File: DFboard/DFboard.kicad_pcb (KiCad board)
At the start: 2 copper layers, 63.5 x 157.5 mm, 20 parts, among them J1 HFBR-2522ETZ, J10 HFBR-1522ETZ, J11 HFBR-2522ETZ, J12 HFBR-1522ETZ, J13 110-43-648-41-001000, J2 HFBR-1522ETZ, J3 HFBR-2522ETZ, J4 HFBR-1522ETZ, J5 HFBR-2522ETZ, J6 HFBR-1522ETZ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

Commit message: Added test points to schematic.  Started pcb layout.
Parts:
- removed J10, J12, J4, J6, J8: HFBR-1522ETZ, OptoDevice:Broadcom_AFBR-16xxZ_Horizontal
- removed J11, J3, J5, J7, J9: HFBR-2522ETZ, OptoDevice:Broadcom_AFBR-16xxZ_Horizontal
- removed R1, R2, R3, R4, R5, R6: 50, Resistor_THT:R_Axial_DIN0207_L6.3mm_D2.5mm_P7.62mm_Horizontal
- added JP1: Jumper3, Connector_PinHeader_2.54mm:PinHeader_1x03_P2.54mm_Vertical, F.Cu at (45.5, 27.5)
- added JP2: Jumper_3_Bridged12, Connector_PinHeader_2.54mm:PinHeader_1x03_P2.54mm_Vertical, F.Cu at (59.0, 33.0)
- added JP3: Jumper3, Connector_PinHeader_2.54mm:PinHeader_1x03_P2.54mm_Vertical, F.Cu at (99.0, 44.0)
- added JP4: Jumper3, Connector_PinHeader_2.54mm:PinHeader_1x03_P2.54mm_Vertical, F.Cu at (128.0, 49.5)
- added JP5: Jumper_3_Bridged12, Connector_PinHeader_2.54mm:PinHeader_1x03_P2.54mm_Vertical, F.Cu at (111.0, 45.0)
- added JP6: Jumper_3_Bridged12, Connector_PinHeader_2.54mm:PinHeader_1x03_P2.54mm_Vertical, F.Cu at (139.5, 47.0)
- added JP7: Jumper_3_Bridged12, Connector_PinHeader_2.54mm:PinHeader_1x03_P2.54mm_Vertical, F.Cu at (168.0, 56.0)
- added JP8: Jumper_2_Bridged, Connector_PinHeader_2.54mm:PinHeader_1x02_P2.54mm_Vertical, F.Cu at (81.2, 43.0)
- added JP9: Jumper_2_Bridged, Connector_PinHeader_2.54mm:PinHeader_1x02_P2.54mm_Vertical, F.Cu at (81.2, 38.5)
- added TP1: RX1, Connector_PinHeader_2.54mm:PinHeader_1x01_P2.54mm_Vertical, F.Cu at (66.5, 98.0)
- added TP10: RX8, Connector_PinHeader_2.54mm:PinHeader_1x01_P2.54mm_Vertical, F.Cu at (166.5, 98.0)
- added TP11: RX6, Connector_PinHeader_2.54mm:PinHeader_1x01_P2.54mm_Vertical, F.Cu at (103.0, 98.0)
- added TP12: RX5, Connector_PinHeader_2.54mm:PinHeader_1x01_P2.54mm_Vertical, F.Cu at (71.0, 98.0)
- added TP13: TX6, Connector_PinHeader_2.54mm:PinHeader_1x01_P2.54mm_Vertical, F.Cu at (104.5, 169.5)
- added TP14: TX5, Connector_PinHeader_2.54mm:PinHeader_1x01_P2.54mm_Vertical, F.Cu at (138.5, 147.0)
- added TP2: TX1, Connector_PinHeader_2.54mm:PinHeader_1x01_P2.54mm_Vertical, F.Cu at (61.5, 98.0)
- added TP3: RX2, Connector_PinHeader_2.54mm:PinHeader_1x01_P2.54mm_Vertical, F.Cu at (98.5, 98.0)
- added TP4: TX2, Connector_PinHeader_2.54mm:PinHeader_1x01_P2.54mm_Vertical, F.Cu at (93.5, 98.0)
- added TP5: RX3, Connector_PinHeader_2.54mm:PinHeader_1x01_P2.54mm_Vertical, F.Cu at (132.0, 97.5)
- added TP6: TX3, Connector_PinHeader_2.54mm:PinHeader_1x01_P2.54mm_Vertical, F.Cu at (127.0, 97.5)
- added TP7: RX4, Connector_PinHeader_2.54mm:PinHeader_1x01_P2.54mm_Vertical, F.Cu at (162.0, 98.0)
- added TP8: TX4, Connector_PinHeader_2.54mm:PinHeader_1x01_P2.54mm_Vertical, F.Cu at (156.5, 98.0)
- added TP9: RX7, Connector_PinHeader_2.54mm:PinHeader_1x01_P2.54mm_Vertical, F.Cu at (136.5, 97.5)
- added U2: ~, Misc:Max3232, F.Cu at (46.6, 74.8)
- added U3: ~, Misc:Max3232, F.Cu at (78.0, 75.0)
- added U4: ~, Misc:Max3232, F.Cu at (111.5, 75.0)
- added U5: ~, Misc:Max3232, F.Cu at (141.4, 75.5)
- added U6: Power, Misc:PowerPal, F.Cu at (271.5, 123.0)
- J1: value HFBR-2522ETZ -> DB25_Plug_MountingHoles_Male; footprint OptoDevice:Broadcom_AFBR-16xxZ_Horizontal -> Connector_Dsub:DSUB-25_Male_Horizontal_P2.77x2.84mm_EdgePinOffset4.94mm_Housed_MountingHolesOffset7.48mm
- J2: value HFBR-1522ETZ -> DB25_Receptacle_MountingHoles_Female; footprint OptoDevice:Broadcom_AFBR-16xxZ_Horizontal -> Connector_Dsub:DSUB-25_Female_Horizontal_P2.77x2.84mm_EdgePinOffset4.94mm_Housed_MountingHolesOffset7.48mm
- moved J2 127.0 mm to (179.7, 27.9), turned to 90 degrees
- moved J13 108.2 mm to (136.0, 117.3), turned to -90 degrees
- moved U1 43.5 mm to (54.0, 96.0)
- moved J1 22.6 mm to (30.8, 28.4), turned to -90 degrees
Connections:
- J1 pad 1: /RX1 -> Net-(U2-R1_In)
- J1 pad 2: Net-(J1-Pad2) -> unconnected-(J1-Pad2)
- J1 pad 3: Net-(U1-Pad10) -> Net-(U3-R1_In)
- J1 pad 4: /RX1 -> unconnected-(J1-Pad4)
- J1 pad 5: (no net) -> Net-(JP9-B)
- J1 pad 8: (no net) -> Net-(JP5-C)
- J13 pad 1: Net-(J1-Pad2) -> Net-(J13-Pad1)
- J13 pad 16: /TX6 -> Net-(J13-Pad16)
- J13 pad 20: unconnected-(J13-Pad20) -> Net-(U4-R2_Out)
- J13 pad 26: unconnected-(J13-Pad26) -> Net-(U5-R2_Out)
- J13 pad 48: unconnected-(J13-Pad48) -> Net-(J13-Pad48)
- J2 pad 1: Net-(J2-Pad1) -> Net-(U2-R1_In)
- J2 pad 2: /TX1 -> unconnected-(J2-Pad2)
- J2 pad 3: unconnected-(J2-Pad3) -> Net-(U3-R1_In)
- J2 pad 5: (no net) -> Net-(JP9-A)
- J2 pad 8: (no net) -> Net-(JP5-A)
- U1 pad 1: unconnected-(U1-Pad1) -> GND
- U1 pad 10: Net-(U1-Pad10) -> Net-(U2-3-5.5V)
- U1 pad 11: unconnected-(U1-Pad11) -> Net-(J13-Pad48)
- U1 pad 8: unconnected-(U1-Pad8) -> Net-(J13-Pad1)
- U1 pad 9: Net-(J1-Pad2) -> Net-(U2-GND)
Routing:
- net Net-(U1-Pad10): track 281.4 -> 0.00 mm
- net Net-(J1-Pad2): track 206.9 -> 0.00 mm
- net /TX6: track 136.7 -> 0.00 mm, vias 1 -> 0
- net /TX5: track 135.1 -> 0.00 mm, vias 3 -> 0
- net /RX5: track 134.0 -> 0.00 mm, vias 3 -> 0
- net /RX6: track 127.4 -> 0.00 mm, vias 3 -> 0
- net /TX4: track 108.8 -> 0.00 mm, vias 3 -> 0
- net /RX4: track 103.3 -> 0.00 mm, vias 4 -> 0
- net /TX3: track 78.6 -> 0.00 mm, vias 1 -> 0
- net /RX3: track 76.2 -> 0.00 mm, vias 1 -> 0
- net /RX2: track 44.6 -> 0.00 mm, vias 1 -> 0
- net /RX1: track 43.2 -> 0.00 mm
- net /TX2: track 35.9 -> 0.00 mm
- net /TX1: track 31.7 -> 0.00 mm
- net Net-(J2-Pad1): track 6.34 -> 0.00 mm
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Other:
- board text removed: "UART1"
- board text removed: "UART2"
- board text removed: "UART3"
- board text removed: "UART4"
- board text removed: "UART5"
- board text removed: "UART6"

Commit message: Submitted board to PCB house
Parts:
- moved U6 111.7 mm to (164.3, 91.6)
- moved TP13 70.0 mm to (56.0, 119.0)
- moved TP10 28.0 mm to (138.7, 94.7)
- moved TP7 28.0 mm to (134.2, 94.7)
- moved TP8 28.0 mm to (128.7, 94.7)
- moved TP14 26.2 mm to (136.5, 120.9)
- moved TP5 20.7 mm to (111.4, 95.0)
- moved TP6 20.7 mm to (106.4, 95.0)
- moved TP9 20.7 mm to (115.9, 95.0)
- moved TP11 20.3 mm to (82.8, 95.9)
- moved TP3 20.3 mm to (78.3, 95.9)
- moved TP4 20.3 mm to (73.3, 95.9)
- moved J2 20.1 mm to (159.7, 25.5)
- moved JP7 18.8 mm to (149.2, 56.0)
- moved J13 15.5 mm to (123.2, 108.5)
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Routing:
- net GND: track 0.00 -> 275.0 mm, vias 0 -> 2
- net Net-(U2-R1_In): track 0.00 -> 188.1 mm, vias 0 -> 2
- net Net-(U3-R1_In): track 0.00 -> 183.1 mm, vias 0 -> 3
- net Net-(U4-R1_In): track 0.00 -> 176.2 mm, vias 0 -> 4
- net Net-(J2-P14): track 0.00 -> 173.7 mm, vias 0 -> 2
- net Net-(U5-R1_In): track 0.00 -> 164.7 mm, vias 0 -> 4
- net Net-(J1-P23): track 0.00 -> 161.1 mm
- net Net-(U2-3-5.5V): track 0.00 -> 149.0 mm
- net Net-(U2-GND): track 0.00 -> 142.7 mm, vias 0 -> 8
- net Net-(J2-P16): track 0.00 -> 142.3 mm, vias 0 -> 1
- net Net-(U5-R2_Out): track 0.00 -> 134.2 mm
- net Net-(J13-Pad48): track 0.00 -> 130.2 mm, vias 0 -> 1
- net Net-(J1-P21): track 0.00 -> 120.7 mm, vias 0 -> 1
- net Net-(J13-Pad1): track 0.00 -> 115.5 mm
- net Net-(J1-P22): track 0.00 -> 105.6 mm
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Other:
- board size 63.5 x 157.5 mm -> 146.7 x 121.9 mm
- board text added: "Data Flow Debugging Board Board version: 0.1 Date: 11/17/2025 Author: Dennis Rossman"
- board text added: "Jumpers 1, 2, 3, 4, 5, 6, 7: Top position is pass through Bottom position is control"
- board text added: "RX1"
- board text added: "RX2"
- board text added: "RX3"
- board text added: "RX4"
- board text added: "RX5"
- board text added: "RX6"
- board text added: "RX7"
- board text added: "RX8"
- board text added: "TX1"
- board text added: "TX2"
- board text added: "TX3"
- board text added: "TX4"
- board text added: "TX5"
- board text added: "TX6"
- board text removed: "Implanter Fiber Optic Interface Board version: 0.1 Date: 1/5/2023 Author: Dennis Rossman"

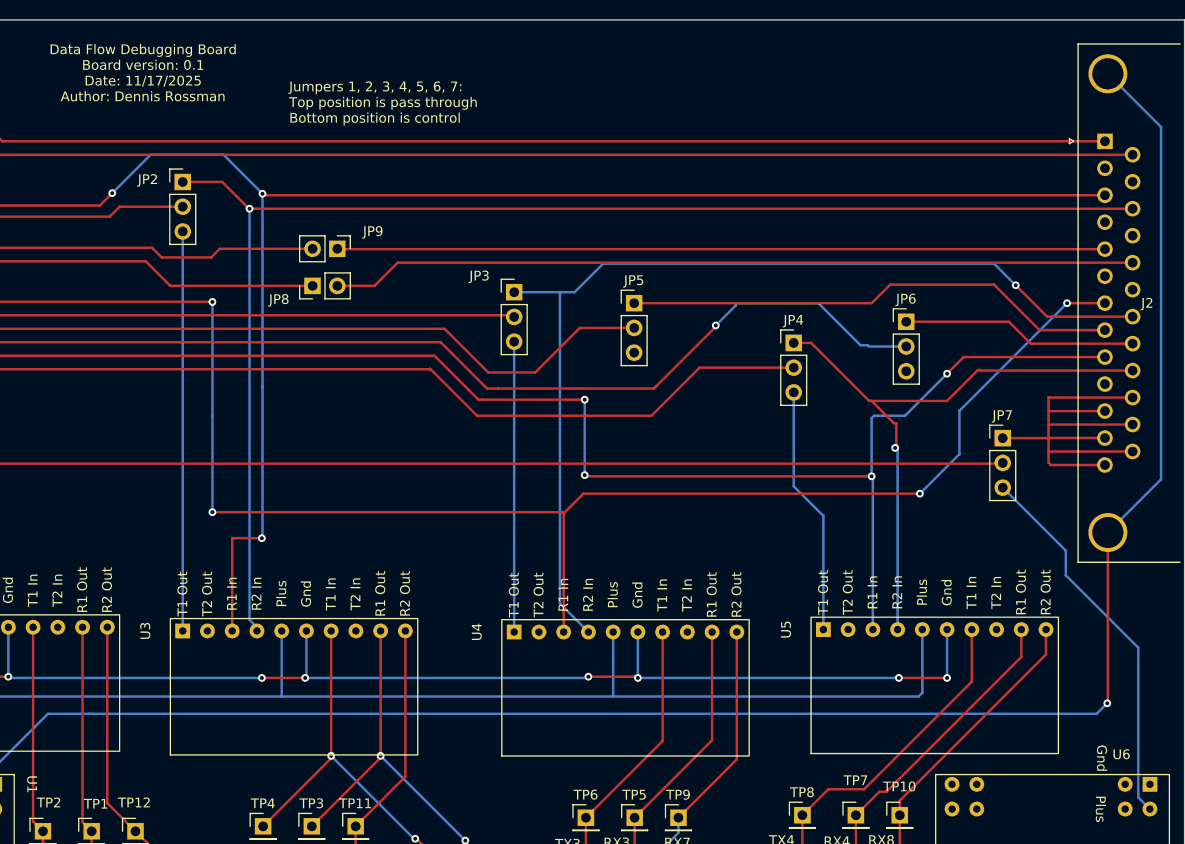
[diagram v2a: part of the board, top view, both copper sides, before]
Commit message: Board version 0.2 - fixed missing ground
The ground for the PowerPal was not connected to the ground coming from the implanter and the signals were all over the place.
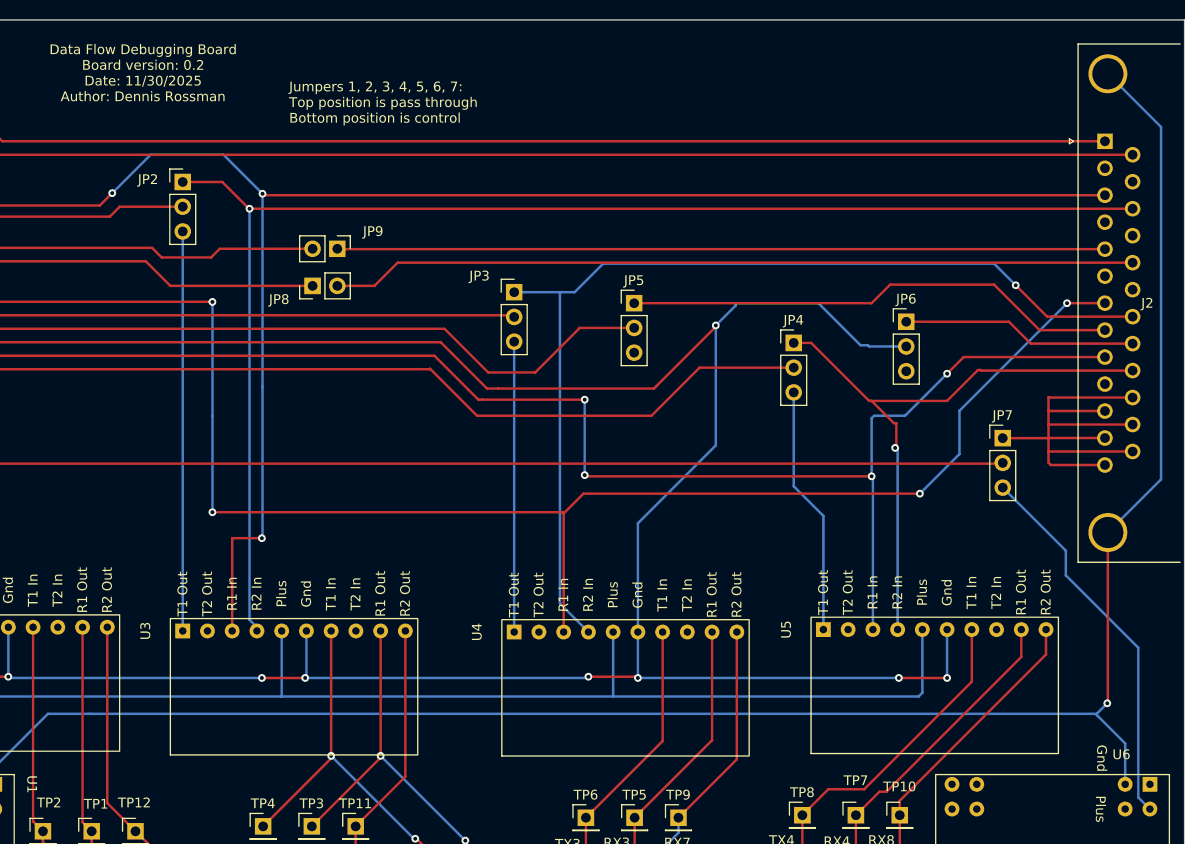
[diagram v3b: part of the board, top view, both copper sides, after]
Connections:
- U1 pad 9: Net-(U2-GND) -> Net-(J1-P21)
- U2 pad 6: Net-(U2-GND) -> Net-(J1-P21)
- U3 pad 6: Net-(U2-GND) -> Net-(J1-P21)
- U4 pad 6: Net-(U2-GND) -> Net-(J1-P21)
- U5 pad 6: Net-(U2-GND) -> Net-(J1-P21)
- U6 pad 2: unconnected-(U6-Ground-Pad2) -> Net-(J1-P21)
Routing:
- net Net-(J1-P21): track 120.7 -> 298.2 mm, vias 1 -> 9
- net Net-(U2-GND): track 142.7 -> 0.00 mm, vias 8 -> 0
- net GND: track 275.0 -> 283.5 mm
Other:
- board text added: "Data Flow Debugging Board Board version: 0.2 Date: 11/30/2025 Author: Dennis Rossman"
- board text removed: "Data Flow Debugging Board Board version: 0.1 Date: 11/17/2025 Author: Dennis Rossman"
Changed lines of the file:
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@@
 		(allow_soldermask_bridges_in_footprints no)
 		(pcbplotparams
-			(layerselection 0x00010f0_ffffffff)
+			(layerselection 0x00010e0_ffffffff)
 			(plot_on_all_layers_selection 0x0000000_00000000)
 			(disableapertmacros no)
@@
 	(net 63 "unconnected-(J1-P17-Pad17)")
 	(net 64 "Net-(U5-R1_In)")
-	(net 65 "Net-(J1-P21)")
+	(net 65 "unconnected-(U6-Ground-Pad1)")
 	(net 66 "Net-(J2-P23)")
 	(net 67 "unconnected-(J2-P15-Pad15)")
@@
 	(net 95 "Net-(U2-3-5.5V)")
 	(net 96 "unconnected-(U1-3.3V-Pad18)")
-	(net 97 "Net-(U2-GND)")
+	(net 97 "Net-(J1-P21)")
 	(net 98 "unconnected-(U2-T2_In-Pad8)")
 	(net 99 "unconnected-(U2-T2_Out-Pad2)")
@@
 	(net 108 "unconnected-(U6-3.3V-Pad17)")
 	(net 109 "unconnected-(U6-3.3V-Pad10)")
-	(net 110 "unconnected-(U6-Ground-Pad1)")
-	(net 111 "unconnected-(U6-3.3V-Pad11)")
-	(net 112 "unconnected-(U6-Ground-Pad2)")
+	(net 110 "unconnected-(U6-3.3V-Pad11)")
 	(footprint "Connector_PinHeader_2.54mm:PinHeader_1x03_P2.54mm_Vertical"
 		(layer "F.Cu")
@@
 			(layers "*.Cu" "*.Mask")
 			(remove_unused_layers no)
-			(net 110 "unconnected-(U6-Ground-Pad1)")
+			(net 65 "unconnected-(U6-Ground-Pad1)")
 			(pinfunction "Ground")
 			(pintype "power_out+no_connect")
@@
 			(layers "*.Cu" "*.Mask")
 			(remove_unused_layers no)
-			(net 112 "unconnected-(U6-Ground-Pad2)")
+			(net 97 "Net-(J1-P21)")
 			(pinfunction "Ground")
-			(pintype "power_out+no_connect")
+			(pintype "power_out")
 		)
 		(pad "8" thru_hole circle
@@
 			(layers "*.Cu" "*.Mask")
 			(remove_unused_layers no)
-			(net 111 "unconnected-(U6-3.3V-Pad11)")
+			(net 110 "unconnected-(U6-3.3V-Pad11)")
 			(pinfunction "3.3V")
 			(pintype "power_out+no_connect")
@@
 			(layers "*.Cu" "*.Mask")
 			(remove_unused_layers no)
-			(net 97 "Net-(U2-GND)")
+			(net 97 "Net-(J1-P21)")
 			(pinfunction "GND")
 			(pintype "input")
@@
 			(layers "*.Cu" "*.Mask")
 			(remove_unused_layers no)
-			(net 65 "Net-(J1-P21)")
+			(net 97 "Net-(J1-P21)")
 			(pinfunction "P21")
 			(pintype "passive")
@@
 			(layers "*.Cu" "*.Mask")
 			(remove_unused_layers no)
-			(net 97 "Net-(U2-GND)")
+			(net 97 "Net-(J1-P21)")
 			(pinfunction "Ground")
 			(pintype "power_out")
@@
 			(layers "*.Cu" "*.Mask")
 			(remove_unused_layers no)
-			(net 97 "Net-(U2-GND)")
+			(net 97 "Net-(J1-P21)")
 			(pinfunction "GND")
 			(pintype "input")
@@
 			(layers "*.Cu" "*.Mask")
 			(remove_unused_layers no)
-			(net 97 "Net-(U2-GND)")
+			(net 97 "Net-(J1-P21)")
 			(pinfunction "GND")
 			(pintype "input")
@@
 			(layers "*.Cu" "*.Mask")
 			(remove_unused_layers no)
-			(net 65 "Net-(J1-P21)")
+			(net 97 "Net-(J1-P21)")
 			(pinfunction "C")
 			(pintype "passive")
@@
 			(layers "*.Cu" "*.Mask")
 			(remove_unused_layers no)
-			(net 97 "Net-(U2-GND)")
+			(net 97 "Net-(J1-P21)")
 			(pinfunction "GND")
 			(pintype "input")
@@
 		)
 	)
-	(gr_text "Data Flow Debugging Board\nBoard version: 0.1\nDate: 11/17/2025\nAuthor: Dennis Rossman"
+	(gr_text "Data Flow Debugging Board\nBoard version: 0.2\nDate: 11/30/2025\nAuthor: Dennis Rossman"
 		(at 60.96 18.542 0)
 		(layer "F.SilkS")
@@
 	)
 	(segment
+		(start 161.798 87.376)
+		(end 161.798 91.567)
+		(width 0.254)
+		(layer "B.Cu")
+		(net 57)
+	)
+	(segment
 		(start 51.181 84.328)
 		(end 55.499 84.328)
@@
 	)
 	(segment
+		(start 158.877 84.328)
+		(end 158.877 84.455)
+		(width 0.254)
+		(layer "B.Cu")
+		(net 57)
+	)
+	(segment
+		(start 158.877 84.455)
+		(end 161.798 87.376)
+		(width 0.254)
+		(layer "B.Cu")
+		(net 57)
+	)
+	(segment
 		(start 165.481 24.07)
 		(end 165.481 60.248)
@@
 	)
 	(segment
-		(start 113.411 50.927)
-		(end 113.665 50.673)
-		(width 0.254)
-		(layer "F.Cu")
-		(net 65)
-	)
-	(segment
-		(start 91.514 46.175)
-		(end 92.71 47.371)
-		(width 0.254)
-		(layer "F.Cu")
-		(net 65)
-	)
-	(segment
-		(start 97.409 50.927)
-		(end 113.411 50.927)
-		(width 0.254)
-		(layer "F.Cu")
-		(net 65)
-	)
-	(segment
-		(start 96.266 50.927)
-		(end 97.409 50.927)
-		(width 0.254)
-		(layer "F.Cu")
-		(net 65)
-	)
-	(segment
-		(start 26.243 46.175)
-		(end 91.514 46.175)
-		(width 0.254)
-		(layer "F.Cu")
-		(net 65)
-	)
-	(segment
-		(start 92.71 47.371)
-		(end 96.266 50.927)
-		(width 0.254)
-		(layer "F.Cu")
-		(net 65)
-	)
-	(segment
-		(start 113.665 50.673)
-		(end 119.761 44.577)
-		(width 0.254)
-		(layer "F.Cu")
-		(net 65)
-	)
-	(segment
-		(start 119.761 44.577)
-		(end 119.761 44.45)
-		(width 0.254)
-		(layer "F.Cu")
-		(net 65)
-	)
-	(via
-		(at 119.761 44.45)
-		(size 0.8)
-		(drill 0.4)
-		(layers "F.Cu" "B.Cu")
-		(net 65)
-	)
-	(segment
-		(start 130.302 42.164)
-		(end 134.62 46.482)
-		(width 0.254)
-		(layer "B.Cu")
-		(net 65)
-	)
-	(segment
-		(start 135.382 46.482)
-		(end 135.509 46.609)
-		(width 0.254)
-		(layer "B.Cu")
-		(net 65)
-	)
-	(segment
-		(start 119.761 44.45)
-		(end 121.793 42.418)
-		(width 0.254)
-		(layer "B.Cu")
-		(net 65)
-	)
-	(segment
-		(start 121.793 42.164)
-		(end 130.302 42.164)
-		(width 0.254)
-		(layer "B.Cu")
-		(net 65)
-	)
-	(segment
-		(start 121.793 42.418)
-		(end 121.793 42.164)
-		(width 0.254)
-		(layer "B.Cu")
-		(net 65)
-	)
-	(segment
-		(start 134.62 46.482)
-		(end 135.382 46.482)
-		(width 0.254)
-		(layer "B.Cu")
-		(net 65)
-	)
-	(segment
-		(start 135.509 46.609)
-		(end 139.319 46.609)
-		(width 0.254)
-		(layer "B.Cu")
-		(net 65)
-	)
-	(segment
 		(start 153.934 57.394)
 		(end 153.924 57.404)
@@
 	)
 	(segment
+		(start 113.411 50.927)
+		(end 113.665 50.673)
+		(width 0.254)
+		(layer "F.Cu")
+		(net 97)
+	)
+	(segment
 		(start 138.557 80.645)
 		(end 143.51 80.645)
@@
 	)
 	(segment
+		(start 91.514 46.175)
+		(end 92.71 47.371)
+		(width 0.254)
+		(layer "F.Cu")
+		(net 97)
+	)
+	(segment
+		(start 97.409 50.927)
+		(end 113.411 50.927)
+		(width 0.254)
+		(layer "F.Cu")
+		(net 97)
+	)
+	(segment
 		(start 111.633 80.518)
 		(end 111.76 80.645)
@@
 	)
 	(segment
+		(start 96.266 50.927)
+		(end 97.409 50.927)
+		(width 0.254)
+		(layer "F.Cu")
+		(net 97)
+	)
+	(segment
+		(start 26.243 46.175)
+		(end 91.514 46.175)
+		(width 0.254)
+		(layer "F.Cu")
+		(net 97)
+	)
+	(segment
 		(start 106.68 80.518)
 		(end 111.633 80.518)
@@
 	)
 	(segment
+		(start 92.71 47.371)
+		(end 96.266 50.927)
+		(width 0.254)
+		(layer "F.Cu")
+		(net 97)
+	)
+	(segment
+		(start 113.665 50.673)
+		(end 119.761 44.577)
+		(width 0.254)
+		(layer "F.Cu")
+		(net 97)
+	)
+	(segment
+		(start 119.761 44.577)
+		(end 119.761 44.45)
+		(width 0.254)
+		(layer "F.Cu")
+		(net 97)
+	)
+	(segment
 		(start 77.597 80.645)
 		(end 77.724 80.772)
@@
 	)
 	(via
+		(at 119.761 44.45)
+		(size 0.8)
+		(drill 0.4)
+		(layers "F.Cu" "B.Cu")
+		(net 97)
+	)
+	(via
 		(at 111.76 80.645)
 		(size 0.8)
@@
 	)
 	(segment
+		(start 119.761 44.45)
+		(end 119.761 56.769)
+		(width 0.254)
+		(layer "B.Cu")
+		(net 97)
+	)
+	(segment
 		(start 111.76 75.931)
 		(end 111.76 80.645)
@@
 	)
 	(segment
+		(start 111.76 64.77)
+		(end 111.76 75.931)
+		(width 0.254)
+		(layer "B.Cu")
+		(net 97)
+	)
+	(segment
+		(start 119.761 56.769)
+		(end 111.76 64.77)
+		(width 0.254)
+		(layer "B.Cu")
+		(net 97)
+	)
+	(segment
+		(start 130.302 42.164)
+		(end 134.62 46.482)
+		(width 0.254)
+		(layer "B.Cu")
+		(net 97)
+	)
+	(segment
+		(start 135.382 46.482)
+		(end 135.509 46.609)
+		(width 0.254)
+		(layer "B.Cu")
+		(net 97)
+	)
+	(segment
 		(start 77.724 75.819)
 		(end 77.724 80.518)
@@
 	)
 	(segment
+		(start 119.761 44.45)
+		(end 121.793 42.418)
+		(width 0.254)
+		(layer "B.Cu")
+		(net 97)
+	)
+	(segment
+		(start 121.793 42.164)
+		(end 130.302 42.164)
+		(width 0.254)
+		(layer "B.Cu")
+		(net 97)
+	)
+	(segment
+		(start 121.793 42.418)
+		(end 121.793 42.164)
+		(width 0.254)
+		(layer "B.Cu")
+		(net 97)
+	)
+	(segment
 		(start 106.553 80.645)
 		(end 106.68 80.518)
@@
 		(width 0.254)
 		(layer "B.Cu")
+		(net 97)
+	)
+	(segment
+		(start 134.62 46.482)
+		(end 135.382 46.482)
+		(width 0.254)
+		(layer "B.Cu")
+		(net 97)
+	)
+	(segment
+		(start 135.509 46.609)
+		(end 139.319 46.609)
+		(width 0.254)
+		(layer "B.Cu")
